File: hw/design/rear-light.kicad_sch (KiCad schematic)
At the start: 109 parts, among them J1 Conn_ARM_SWD_TagConnect_TC203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, Q501 2N7002, Q502 2N7002, Q503 2N7002, Q601 2N7002, U300 MCP2021A-330E/SN, U400 ATSAMD21E18A-A, U500 TLD2331-3EP, U600 TLD2132-1EP, U700 BMA456

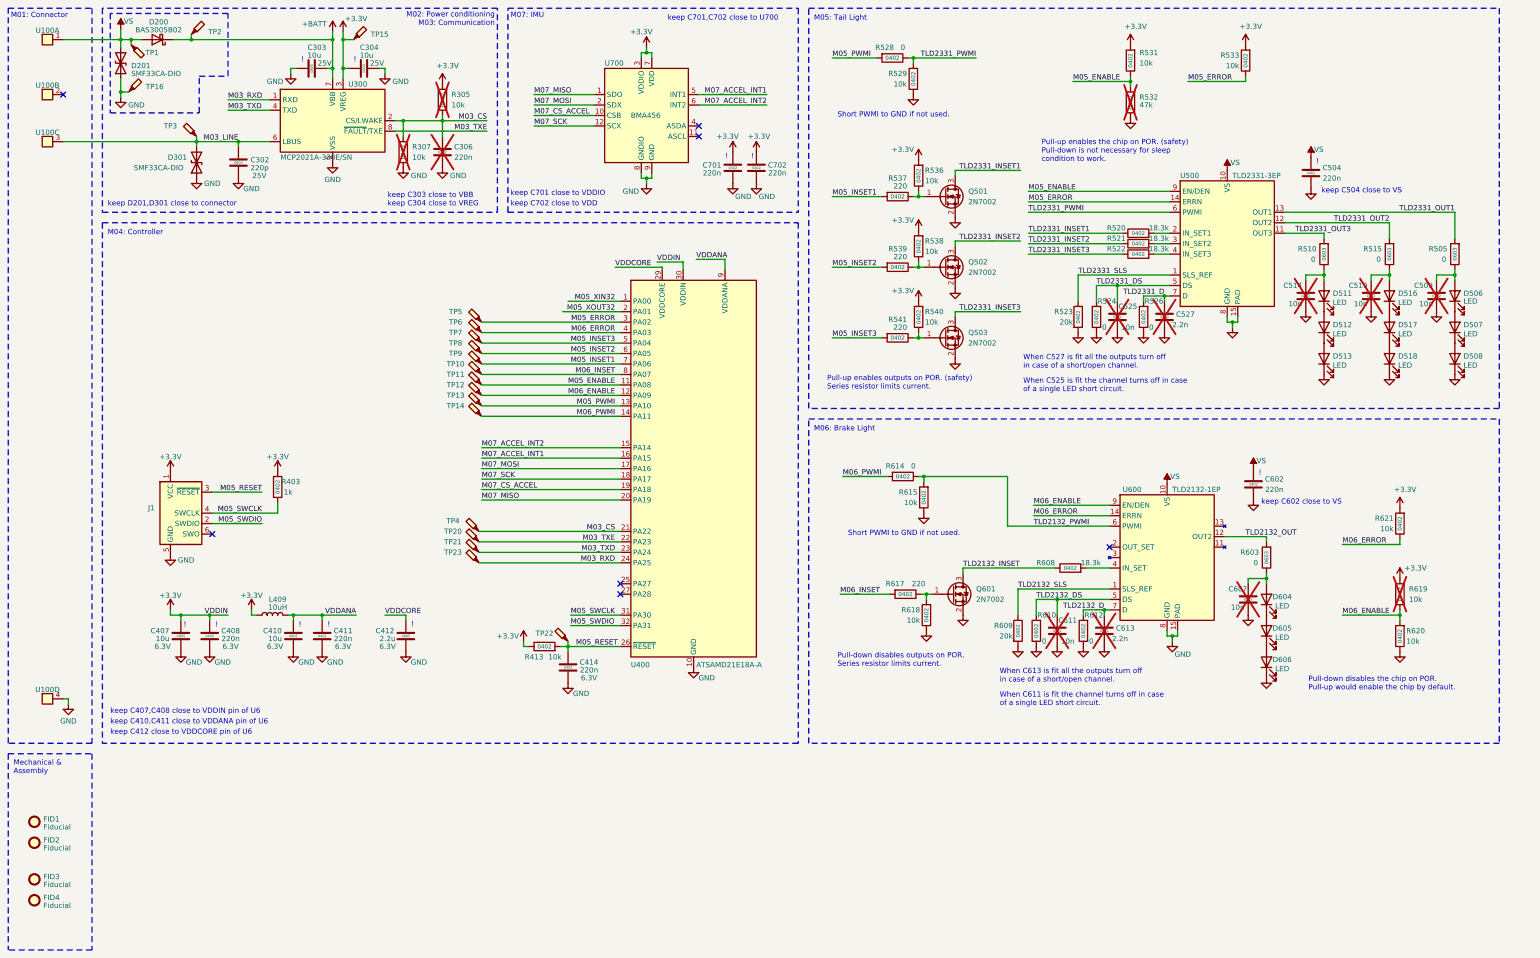
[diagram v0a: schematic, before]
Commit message: Gen1.0 design finalization (#1)
* Final layout for Gen1.0, PCB has been ordered
* Design documentation is mostly done
* Schematic has been completed
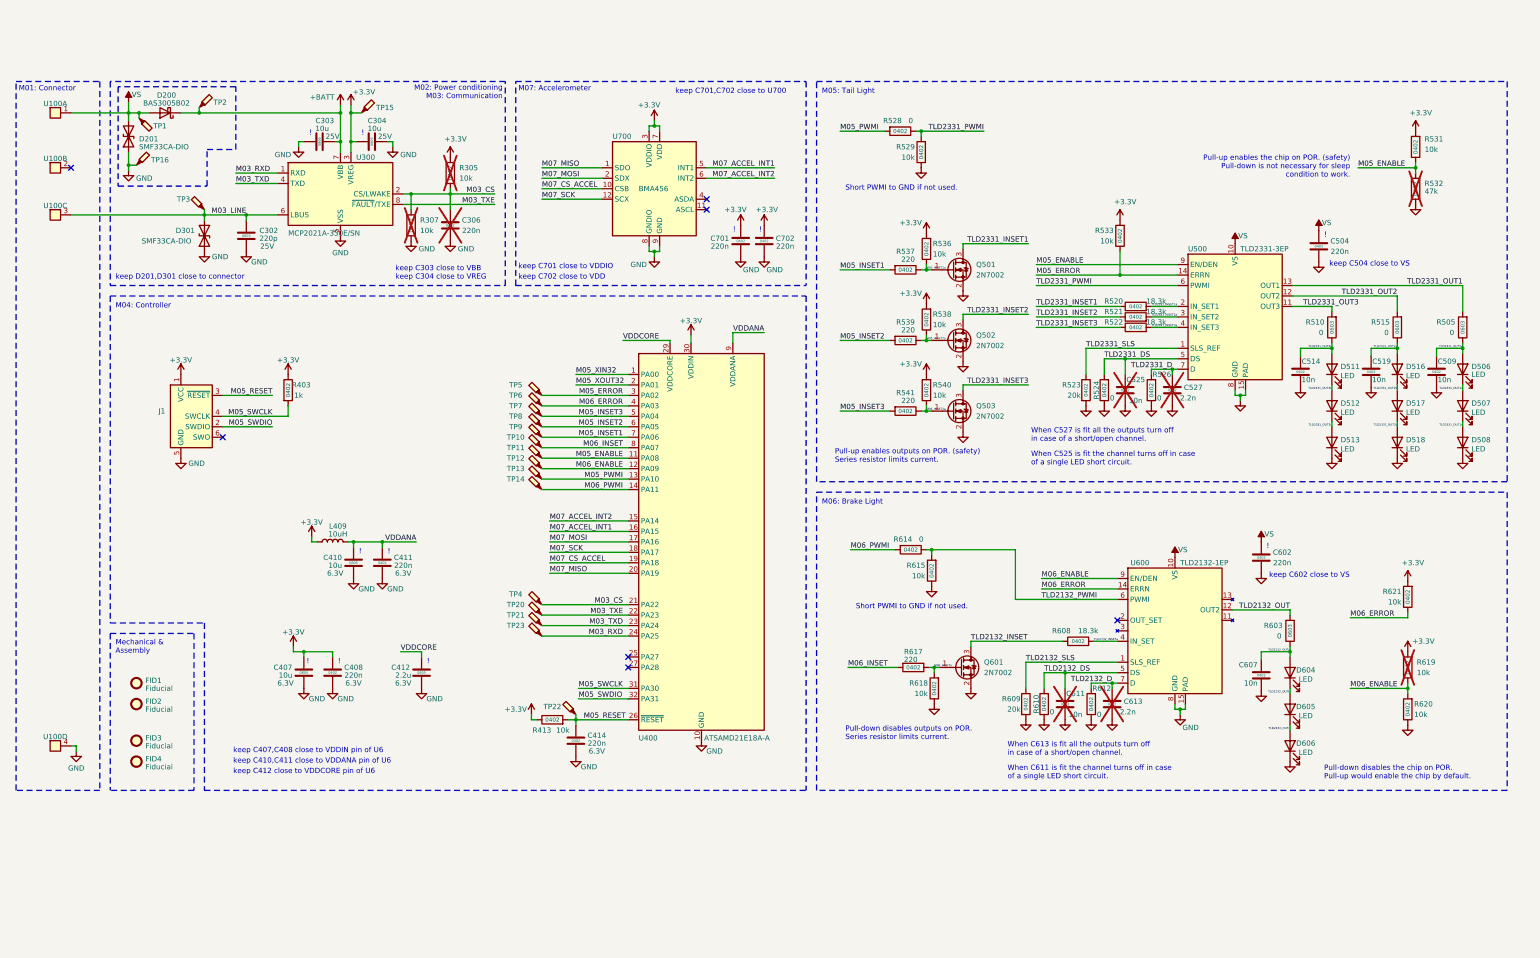
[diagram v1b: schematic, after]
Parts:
- C509, C514, C519, C607: now fitted
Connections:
- net TLD2331_OUT1a: now reaches C509.2, D506.2 (A), R505.1
- net TLD2132_OUTa: now reaches C607.2, D604.2 (A), R603.1
- net TLD2331_OUT2c: now reaches D517.1 (K), D518.2 (A)
- net TLD2331_OUT3b: now reaches D511.1 (K), D512.2 (A)
- net TLD2331_OUT3a: now reaches C514.2, D511.2 (A), R510.1
- net TLD2132_INSETa: now reaches R608.2, U600.4 (IN_SET)
- net TLD2132_OUTb: now reaches D604.1 (K), D605.2 (A)
- net M05_INSET2a: now reaches Q502.1 (G), R538.1, R539.1
- net TLD2331_OUT1c: now reaches D506.1 (K), D507.2 (A)
- net TLD2331_OUT1c: now also D507.1 (K), D508.2 (A)
- net TLD2331_OUT3c: now reaches D512.1 (K), D513.2 (A)
- net TLD2331_OUT2b: now reaches D516.1 (K), D517.2 (A)
- net M05_INSET3a: now reaches Q503.1 (G), R540.1, R541.1
- net M05_INSET1a: now reaches Q501.1 (G), R536.1, R537.1
- net TLD2331_INSET3a: now reaches R522.2, U500.4 (IN_SET3)
- net M06_INSETa: now reaches Q601.1 (G), R617.1, R618.2
- net TLD2132_OUTc: now reaches D605.1 (K), D606.2 (A)
- net TLD2331_OUT2a: now reaches C519.2, D516.2 (A), R515.1
- net TLD2331_INSET2a: now reaches R521.2, U500.3 (IN_SET2)
- net TLD2331_INSET1a: now reaches R520.2, U500.2 (IN_SET1)
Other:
- note added: "M07: Accelerometer"
- note removed: "M07: IMU"
- moved on the sheet: C302, C303, C304, C306, C407, C408, C410, C411, C412, C414, C504, C525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

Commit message: Uploading datasheets (#4)
Changes 220n capacitors to 100n
PWMI pull downs populated according to expected default behavior
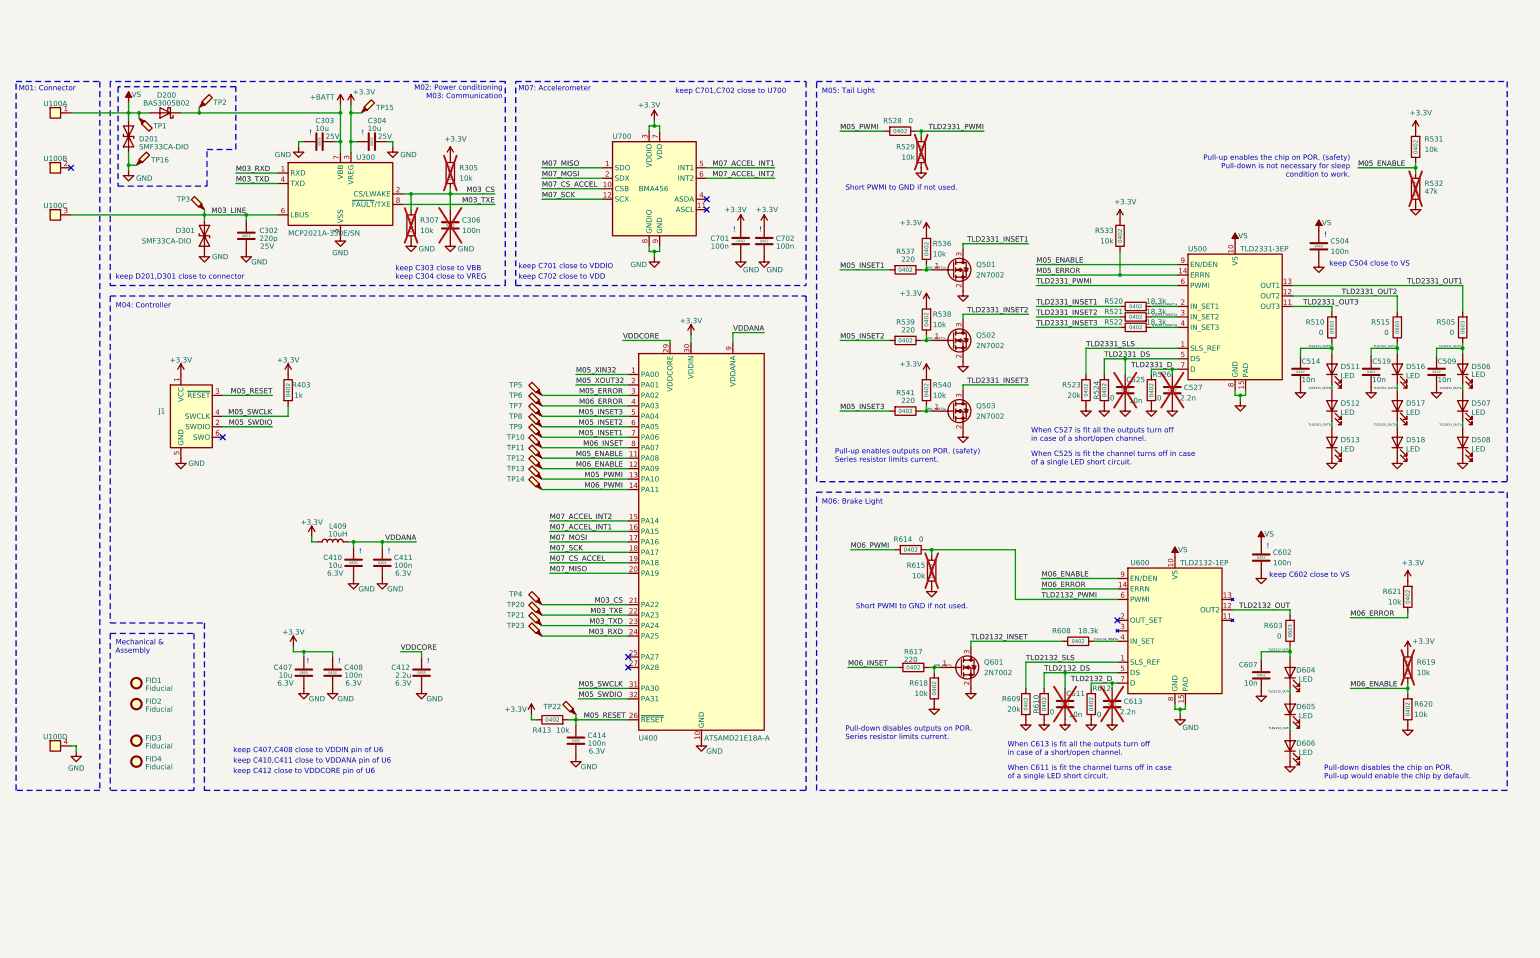
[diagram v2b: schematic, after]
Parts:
- C306, C408, C411, C414, C504, C602, C701, C702: value 220n -> 100n
- R529, R615: now not fitted
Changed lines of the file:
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@@
   )
   (symbol (lib_id "Device:R") (at 251.46 171.45 180) (unit 1)
-    (in_bom yes) (on_board yes) (dnp no)
+    (in_bom yes) (on_board yes) (dnp yes)
     (property "Reference" "R615" (at 247.65 170.18 0)
       (effects (font (size 1.27 1.27)))
@@
       (effects (font (size 1.27 1.27)))
     )
-    (property "Value" "220n" (at 170.18 213.36 0)
+    (property "Value" "100n" (at 170.18 213.36 0)
       (effects (font (size 1.27 1.27)))
     )
@@
       (effects (font (size 1.27 1.27)))
     )
-    (property "Value" "220n" (at 215.9 92.71 0)
+    (property "Value" "100n" (at 215.9 92.71 0)
       (effects (font (size 1.27 1.27)))
     )
@@
       (effects (font (size 1.27 1.27)))
     )
-    (property "Value" "220n" (at 336.55 169.545 0)
+    (property "Value" "100n" (at 336.55 169.545 0)
       (effects (font (size 1.27 1.27)))
     )
@@
       (effects (font (size 1.27 1.27)))
     )
-    (property "Value" "220n" (at 139.7 88.9 0)
+    (property "Value" "100n" (at 139.7 88.9 0)
       (effects (font (size 1.27 1.27)))
     )
@@
   )
   (symbol (lib_id "Device:R") (at 248.92 69.85 180) (unit 1)
-    (in_bom yes) (on_board yes) (dnp no)
+    (in_bom yes) (on_board yes) (dnp yes)
     (property "Reference" "R529" (at 245.11 68.58 0)
       (effects (font (size 1.27 1.27)))
@@
       (effects (font (size 1.27 1.27)))
     )
-    (property "Value" "220n" (at 200.025 92.71 0)
+    (property "Value" "100n" (at 200.025 92.71 0)
       (effects (font (size 1.27 1.27)))
     )
@@
       (effects (font (size 1.27 1.27)))
     )
-    (property "Value" "220n" (at 350.52 93.98 0)
+    (property "Value" "100n" (at 350.52 93.98 0)
       (effects (font (size 1.27 1.27)))
     )
@@
       (effects (font (size 1.27 1.27)))
     )
-    (property "Value" "220n" (at 123.19 170.18 0)
+    (property "Value" "100n" (at 123.19 170.18 0)
       (effects (font (size 1.27 1.27)))
     )
@@
       (effects (font (size 1.27 1.27)))
     )
-    (property "Value" "220n" (at 111.125 196.85 0)
+    (property "Value" "100n" (at 111.125 196.85 0)
       (effects (font (size 1.27 1.27)))
     )
